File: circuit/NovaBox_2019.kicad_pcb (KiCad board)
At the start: 2 copper layers, 100 x 100 mm, 50 parts, among them J1 USB_B, Q1 BC557, Q2 BC547, U1 CSR8635_MODULE, U2 CSR_DebugSmall, U3 TPA3136D2, U4 LM317

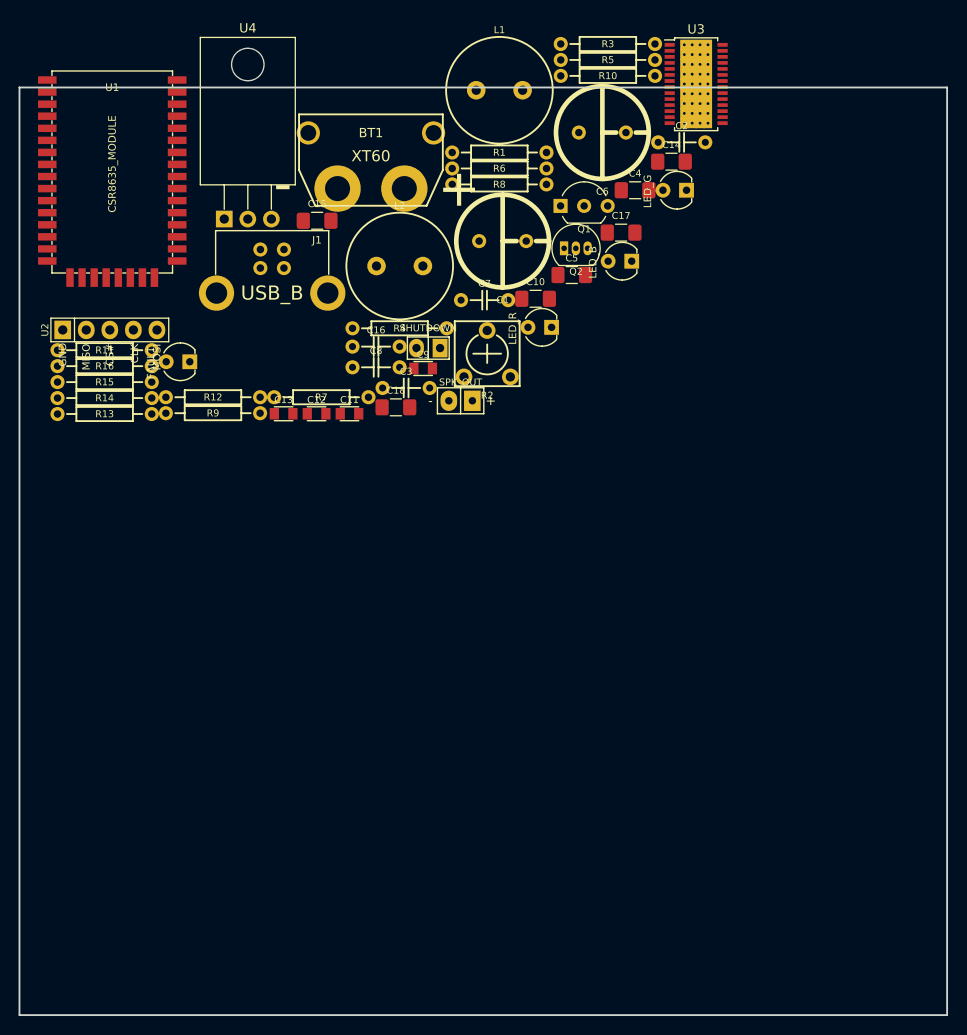
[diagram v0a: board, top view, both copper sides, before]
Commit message: started Power; still need to change transistor on TPA3136; lengthen the pads on HTSSOP
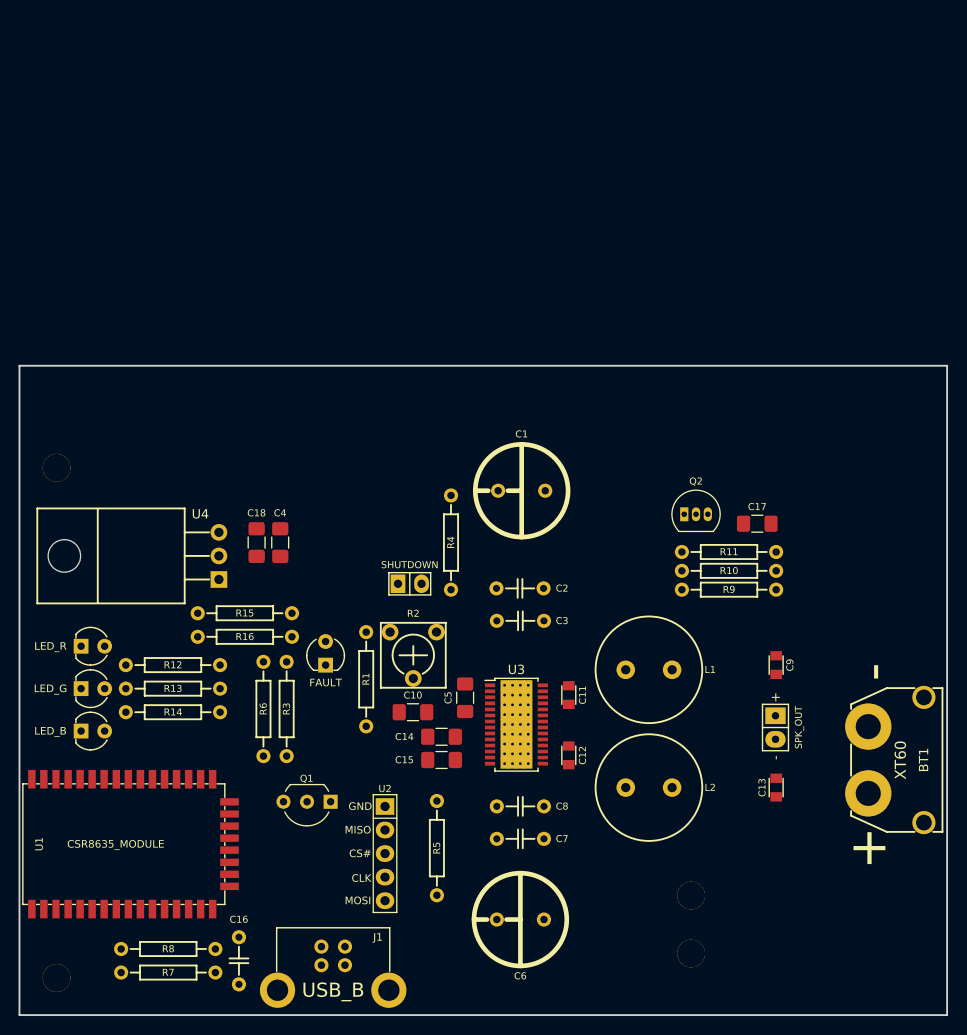
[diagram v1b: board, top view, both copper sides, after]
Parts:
- added J2: HOLE, NovaBox:MountingHole, F.Cu at (54.0, 91.0)
- added J3: HOLE, NovaBox:MountingHole, F.Cu at (54.0, 146.0)
- added J4: HOLE, NovaBox:MountingHole, F.Cu at (122.4, 137.1)
- added J5: HOLE, NovaBox:MountingHole, F.Cu at (122.4, 143.4)
- moved BT1 90.1 mm to (147.5, 122.5), turned to 270 degrees
- moved R8 89.8 mm to (66.0, 142.9)
- moved R5 86.9 mm to (95.0, 132.0), turned to 270 degrees
- moved C6 85.3 mm to (104.0, 139.7), turned to 180 degrees
- moved D3 82.6 mm to (57.9, 114.8), turned to 180 degrees
- moved R3 79.6 mm to (78.8, 117.0), turned to 270 degrees
- moved D4 76.1 mm to (57.9, 119.4), turned to 180 degrees
- moved J1 75.4 mm to (83.8, 147.3)
- moved U3 71.7 mm to (103.6, 118.7)
- moved Q1 70.8 mm to (81.0, 127.0), turned to 180 degrees
- moved R11 70.7 mm to (126.5, 100.1), turned to 180 degrees
- moved C16 67.8 mm to (73.7, 144.1), turned to 270 degrees
- moved C14 66.8 mm to (95.5, 120.0)
- moved C13 66.7 mm to (131.6, 125.5), turned to 90 degrees
- moved L1 64.5 mm to (117.9, 112.8)
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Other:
- board size 100 x 100 mm -> 100 x 70 mm
